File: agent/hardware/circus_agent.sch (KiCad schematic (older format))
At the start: 17 parts

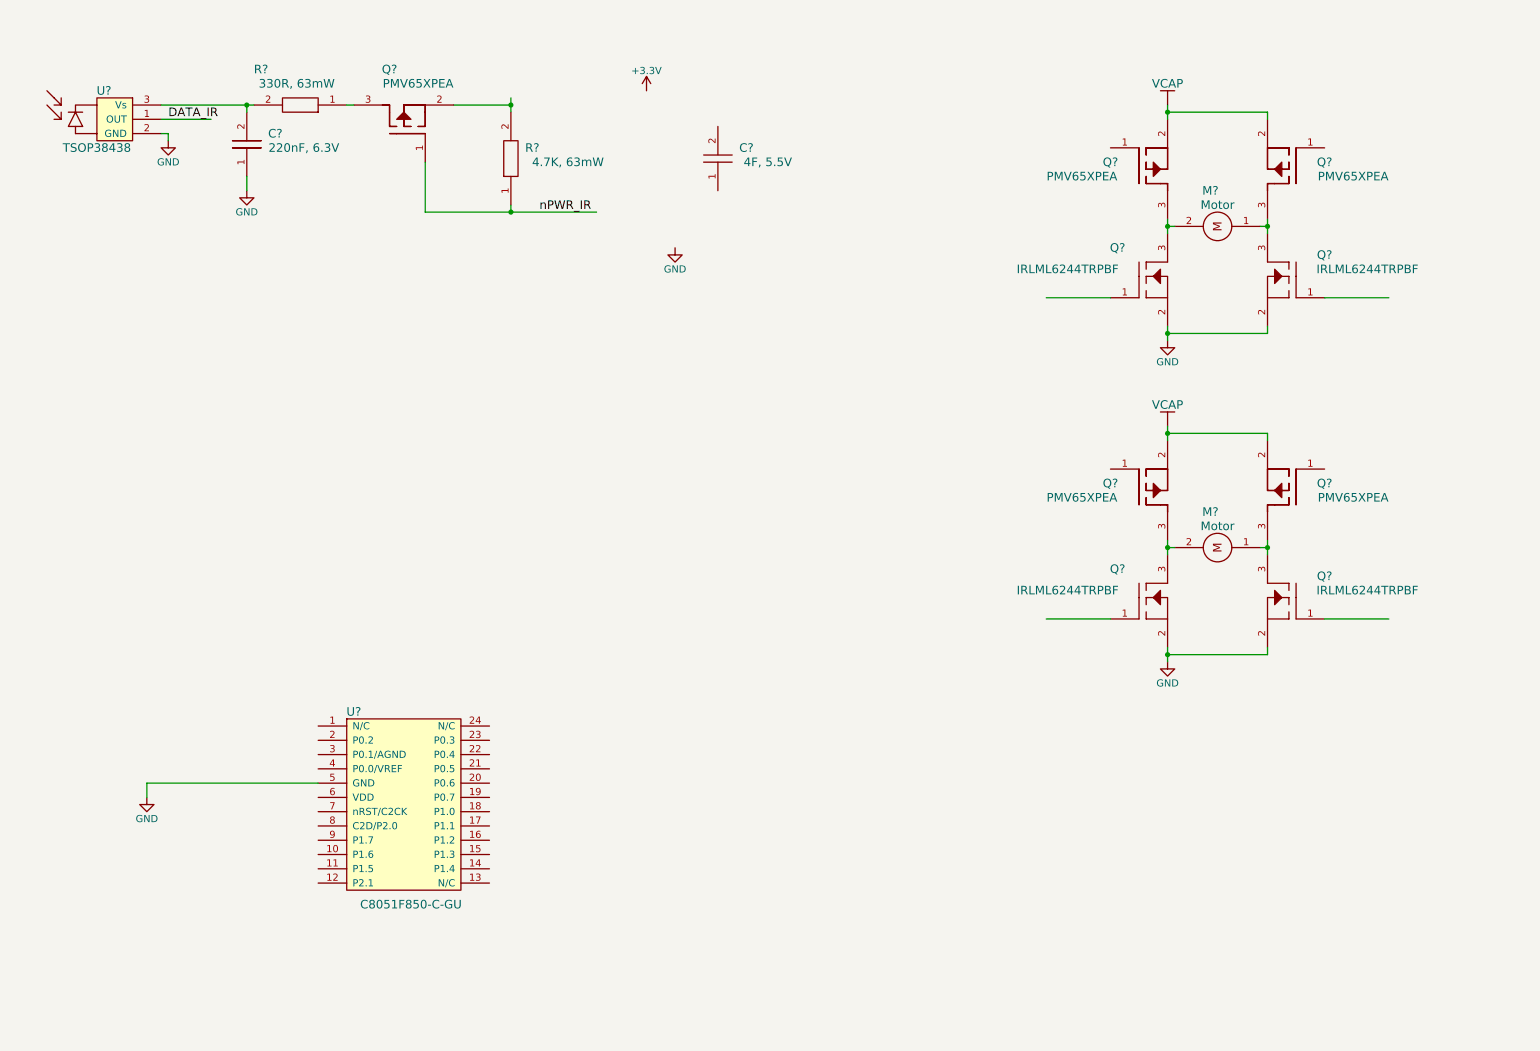
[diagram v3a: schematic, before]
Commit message: Added BJT for highsides
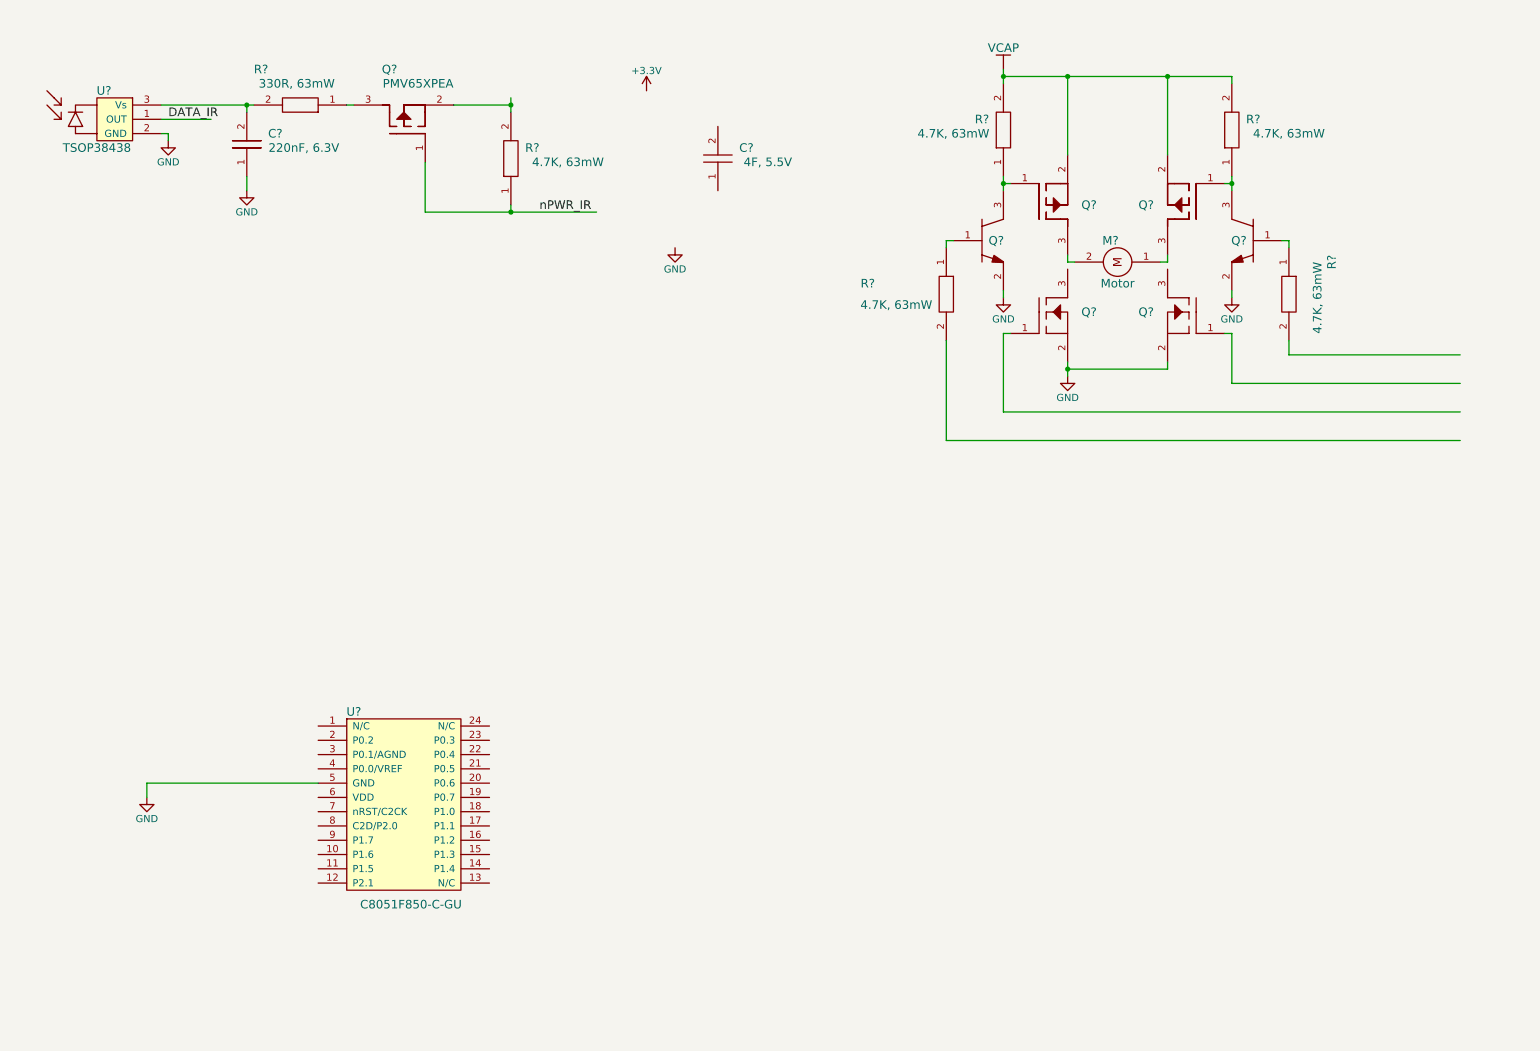
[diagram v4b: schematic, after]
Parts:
- removed M?: Motor, symbol Motor
- removed Q? (x2): PMV65XPEA, symbol PMV65XPEA
- removed Q? (x2): IRLML6244TRPBF, symbol IRLML6244TRPBF
- added Q? (x2): MMBT2222LT1G, symbol MMBT2222LT1G
- added R? (x4): 4.7K, 63mW, symbol CRCW0402330RFKED
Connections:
- wire segments 49 -> 46
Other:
- moved on the sheet: M?, Q?

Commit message: add battery measure and ID
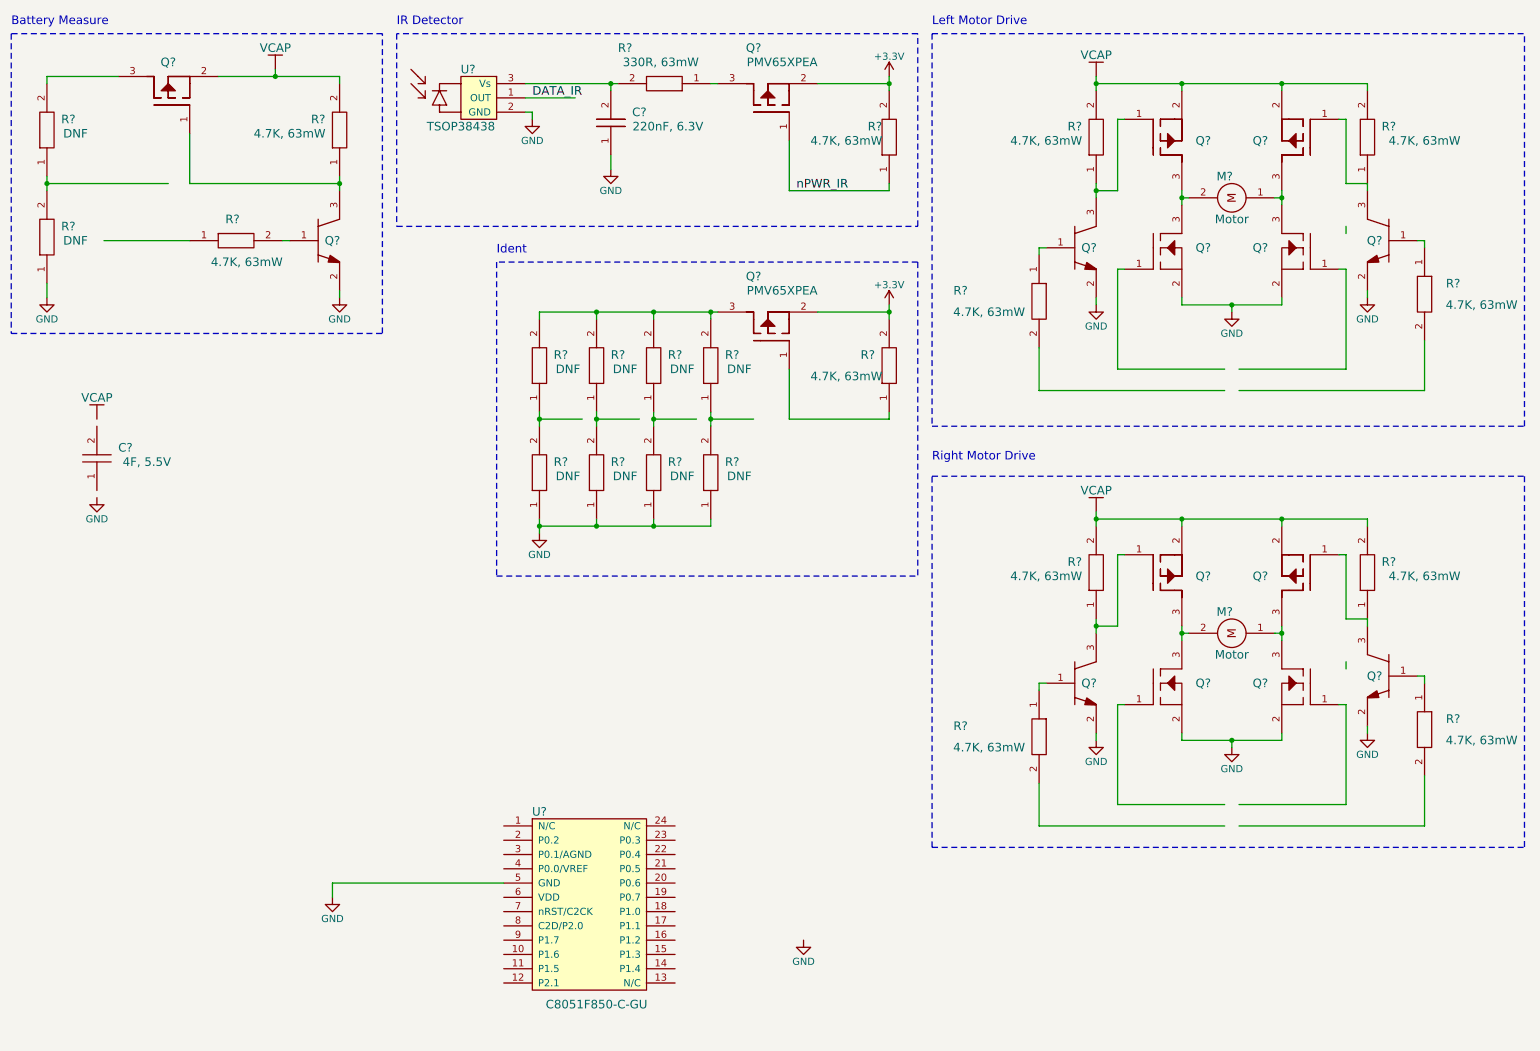
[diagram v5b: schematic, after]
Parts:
- removed C?: 4F, 5.5V, symbol SuperCap
- added C?: 4F, 5.5V, symbol SuperCap
- added M?: Motor, symbol Motor
- added Q? (x4): PMV65XPEA, symbol PMV65XPEA
- added Q? (x2): IRLML6244TRPBF, symbol IRLML6244TRPBF
- added Q? (x3): MMBT2222LT1G, symbol MMBT2222LT1G
- added R? (x7): 4.7K, 63mW, symbol CRCW0402330RFKED
- added R? (x10): DNF, symbol CRCW0402330RFKED
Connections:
- wire segments 46 -> 127
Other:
- note added: "Battery Measure"
- note added: "IR Detector"
- note added: "Ident"
- note added: "Left Motor Drive"
- note added: "Right Motor Drive"
- moved on the sheet: C?, M?, Q?, R?, U?

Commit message: add pdfs and synbols for leds and prog
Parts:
- added C?: 100nF, 6.3V, symbol MC0402X224K6R3CT
- added C?: 1uF, 6.3V, symbol MC0402X224K6R3CT
- added D?: KPA-1606CGCK(GREEN), symbol KPA-1606CGCK(GREEN)
- added D?: KPA-1606ECR(RED), symbol KPA-1606ECR(RED)
- added R? (x3): 1K, symbol CRCW0402330RFKED
- added T?: TestPoint, symbol TestPoint
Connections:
- net labels added: BM, PWR_BM
- wire segments 127 -> 142
- no-connect marks 0 -> 3
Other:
- note added: "Microcontroller"
- moved on the sheet: U?
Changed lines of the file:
@@
 L C8051F850-C-GU U?
 U 1 1 5B327CEA
-P 4000 7150
-F 0 "U?" H 4250 8200 60  0000 C CNN
-F 1 "C8051F850-C-GU" H 4650 6850 60  0000 C CNN
-F 2 "" H 4000 7150 60  0001 C CNN
-F 3 "" H 4000 7150 60  0001 C CNN
-F 4 "SiLabs" H 4000 7150 60  0001 C CNN "Man"
-F 5 "C8051F850-C-GU" H 4000 7150 60  0001 C CNN "PartNum"
-	1    4000 7150
+P 4950 5800
+F 0 "U?" H 5200 6850 60  0000 C CNN
+F 1 "C8051F850-C-GU" H 5600 5500 60  0000 C CNN
+F 2 "" H 4950 5800 60  0001 C CNN
+F 3 "" H 4950 5800 60  0001 C CNN
+F 4 "SiLabs" H 4950 5800 60  0001 C CNN "Man"
+F 5 "C8051F850-C-GU" H 4950 5800 60  0001 C CNN "PartNum"
+	1    4950 5800
 	1    0    0    -1
 $EndComp
@@
 L GND #PWR01
 U 1 1 5B327D75
-P 2800 6700
-F 0 "#PWR01" H 2800 6450 50  0001 C CNN
-F 1 "GND" H 2800 6550 50  0000 C CNN
-F 2 "" H 2800 6700 50  0001 C CNN
-F 3 "" H 2800 6700 50  0001 C CNN
-	1    2800 6700
-	1    0    0    -1
-$EndComp
-Wire Wire Line
-	4000 6600 2800 6600
-Wire Wire Line
-	2800 6600 2800 6700
+P 4100 5100
+F 0 "#PWR01" H 4100 4850 50  0001 C CNN
+F 1 "GND" H 4100 4950 50  0000 C CNN
+F 2 "" H 4100 5100 50  0001 C CNN
+F 3 "" H 4100 5100 50  0001 C CNN
+	1    4100 5100
+	1    0    0    -1
+$EndComp
 $Comp
 L TSOP38438 U?
@@
 nPWR_IR
 $Comp
-L GND #PWR?
-U 1 1 5B32B7AB
-P 6100 7000
-F 0 "#PWR?" H 6100 6750 50  0001 C CNN
-F 1 "GND" H 6100 6850 50  0000 C CNN
-F 2 "" H 6100 7000 50  0001 C CNN
-F 3 "" H 6100 7000 50  0001 C CNN
-	1    6100 7000
-	1    0    0    -1
-$EndComp
-$Comp
 L VCAP #PWR??
 U 1 1 5B333F06
@@
 	800  1650 800  1750
 Wire Wire Line
-	800  1700 1650 1700
-Connection ~ 800  1700
-Wire Wire Line
 	1300 950  800  950
 Wire Wire Line
@@
 Text Notes 550  600  0    60   ~ 0
 Battery Measure
+NoConn ~ 6150 4850
+NoConn ~ 6150 5950
+NoConn ~ 4950 4850
+Wire Wire Line
+	4950 5250 4300 5250
+Wire Wire Line
+	4300 5250 4300 5050
+Wire Wire Line
+	4300 5050 4100 5050
+Wire Wire Line
+	4100 5050 4100 5100
+$Comp
+L MC0402X224K6R3CT C?
+U 1 1 5B36B62A
+P 3150 5850
+F 0 "C?" H 3450 6150 60  0000 C CNN
+F 1 "100nF, 6.3V" H 3650 6050 60  0000 C CNN
+F 2 "" H 3150 5850 60  0001 C CNN
+F 3 "" H 3150 5850 60  0001 C CNN
+F 4 "MULTICOMP" H 3150 5850 60  0001 C CNN "Man"
+F 5 "MC0402X224K6R3CT " H 3150 5850 60  0001 C CNN "PartNum"
+	1    3150 5850
+	1    0    0    -1
+$EndComp
+$Comp
+L MC0402X224K6R3CT C?
+U 1 1 5B36BF9E
+P 2200 5850
+F 0 "C?" H 2500 6150 60  0000 C CNN
+F 1 "1uF, 6.3V" H 2650 6050 60  0000 C CNN
+F 2 "" H 2200 5850 60  0001 C CNN
+F 3 "" H 2200 5850 60  0001 C CNN
+F 4 "MULTICOMP" H 2200 5850 60  0001 C CNN "Man"
+F 5 "MC0402X224K6R3CT " H 2200 5850 60  0001 C CNN "PartNum"
+	1    2200 5850
+	1    0    0    -1
+$EndComp
+$Comp
+L GND #PWR?
+U 1 1 5B36C1ED
+P 3250 5900
+F 0 "#PWR?" H 3250 5650 50  0001 C CNN
+F 1 "GND" H 3250 5750 50  0000 C CNN
+F 2 "" H 3250 5900 50  0001 C CNN
+F 3 "" H 3250 5900 50  0001 C CNN
+	1    3250 5900
+	1    0    0    -1
+$EndComp
+$Comp
+L GND #PWR?
+U 1 1 5B36C312
+P 2300 5900
+F 0 "#PWR?" H 2300 5650 50  0001 C CNN
+F 1 "GND" H 2300 5750 50  0000 C CNN
+F 2 "" H 2300 5900 50  0001 C CNN
+F 3 "" H 2300 5900 50  0001 C CNN
+	1    2300 5900
+	1    0    0    -1
+$EndComp
+Wire Wire Line
+	2300 5350 4950 5350
+Wire Wire Line
+	2300 5300 2300 5400
+Wire Wire Line
+	2300 5850 2300 5900
+Wire Wire Line
+	3250 5400 3250 5350
+Connection ~ 3250 5350
+Wire Wire Line
+	3250 5900 3250 5850
+$Comp
+L +3.3V #PWR?
+U 1 1 5B36CC69
+P 2300 5300
+F 0 "#PWR?" H 2300 5150 50  0001 C CNN
+F 1 "+3.3V" H 2300 5440 50  0000 C CNN
+F 2 "" H 2300 5300 50  0001 C CNN
+F 3 "" H 2300 5300 50  0001 C CNN
+	1    2300 5300
+	1    0    0    -1
+$EndComp
+Connection ~ 2300 5350
+$Comp
+L CRCW0402330RFKED R?
+U 1 1 5B36D9FD
+P 3800 6800
+F 0 "R?" H 4000 7200 60  0000 C CNN
+F 1 "1K" H 4050 7100 60  0000 C CNN
+F 2 "" H 3800 6800 60  0001 C CNN
+F 3 "" H 3800 6800 60  0001 C CNN
+F 4 "VISHAY" V 3800 6800 60  0001 C CNN "MULTICOMP"
+F 5 "MCMR04X4701FTL" V 3800 6800 60  0001 C CNN "PartNum"
+	1    3800 6800
+	1    0    0    -1
+$EndComp
+Wire Wire Line
+	4950 5450 4300 5450
+Wire Wire Line
+	4300 5450 4300 6850
+Wire Wire Line
+	4300 6850 3800 6850
+Wire Wire Line
+	3850 6850 3850 6800
+$Comp
+L CRCW0402330RFKED R?
+U 1 1 5B36DE61
+P 3150 6800
+F 0 "R?" V 3000 7100 60  0000 C CNN
+F 1 "1K" V 3100 7100 60  0000 C CNN
+F 2 "" H 3150 6800 60  0001 C CNN
+F 3 "" H 3150 6800 60  0001 C CNN
+F 4 "VISHAY" V 3150 6800 60  0001 C CNN "MULTICOMP"
+F 5 "MCMR04X4701FTL" V 3150 6800 60  0001 C CNN "PartNum"
+	1    3150 6800
+	0    1    1    0
+$EndComp
+$Comp
+L +3.3V #PWR?
+U 1 1 5B36E010
+P 3850 6100
+F 0 "#PWR?" H 3850 5950 50  0001 C CNN
+F 1 "+3.3V" H 3850 6240 50  0000 C CNN
+F 2 "" H 3850 6100 50  0001 C CNN
+F 3 "" H 3850 6100 50  0001 C CNN
+	1    3850 6100
+	1    0    0    -1
+$EndComp
+$Comp
+L CRCW0402330RFKED R?
+U 1 1 5B36E443
+P 3150 7150
+F 0 "R?" V 3000 7450 60  0000 C CNN
+F 1 "1K" V 3100 7450 60  0000 C CNN
+F 2 "" H 3150 7150 60  0001 C CNN
+F 3 "" H 3150 7150 60  0001 C CNN
+F 4 "VISHAY" V 3150 7150 60  0001 C CNN "MULTICOMP"
+F 5 "MCMR04X4701FTL" V 3150 7150 60  0001 C CNN "PartNum"
+	1    3150 7150
+	0    1    1    0
+$EndComp
+Connection ~ 3850 6850
+Wire Wire Line
+	4950 5550 4400 5550
+Wire Wire Line
+	4400 5550 4400 7200
+Wire Wire Line
+	4400 7200 3800 7200
+Text Label 1250 2100 0    60   ~ 0
+PWR_BM
+Text GLabel 6350 5650 2    60   Input ~ 0
+BM
+Text GLabel 1350 1700 2    60   Input ~ 0
+BM
+Wire Wire Line
+	1350 1700 800  1700
+Connection ~ 800  1700
+$Comp
+L TestPoint T?
+U 1 1 5B374125
+P 4900 5000
+F 0 "T?" V 4950 5350 60  0000 C CNN
+F 1 "TestPoint" H 5200 5100 60  0001 C CNN
+F 2 "" H 4900 5000 60  0001 C CNN
+F 3 "" H 4900 5000 60  0001 C CNN
+	1    4900 5000
+	0    -1   -1   0
+$EndComp
+Wire Wire Line
+	4950 4950 4900 4950
+Wire Notes Line
+	6900 4700 6900 7700
+Wire Notes Line
+	6900 7700 2000 7700
+Wire Notes Line
+	2000 7700 2000 4700
+Wire Notes Line
+	2000 4700 6900 4700
+Text Notes 2000 4650 0    60   ~ 0
+Microcontroller
+$Comp
+L KPA-1606CGCK(GREEN) D?
+U 1 1 5B375D12
+P 700 6100
+F 0 "D?" H 950 6400 60  0000 C CNN
+F 1 "KPA-1606CGCK(GREEN)" H 1450 6300 60  0000 C CNN
+F 2 "" H 700 6100 60  0001 C CNN
+F 3 "" H 700 6100 60  0001 C CNN
+	1    700  6100
+	1    0    0    -1
+$EndComp
+$Comp
+L KPA-1606ECR(RED) D?
+U 1 1 5B375DDB
+P 700 7100
+F 0 "D?" H 950 7400 60  0000 C CNN
+F 1 "KPA-1606ECR(RED)" H 1350 7300 60  0000 C CNN
+F 2 "" H 700 7100 60  0001 C CNN
+F 3 "" H 700 7100 60  0001 C CNN
+	1    700  7100
+	1    0    0    -1
+$EndComp
 $EndSCHEMATC
